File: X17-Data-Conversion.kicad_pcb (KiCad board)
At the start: 2 copper layers, 26 parts, among them J1 Conn_01x05, U2 STM32F091CCTx, U3 MAX485E

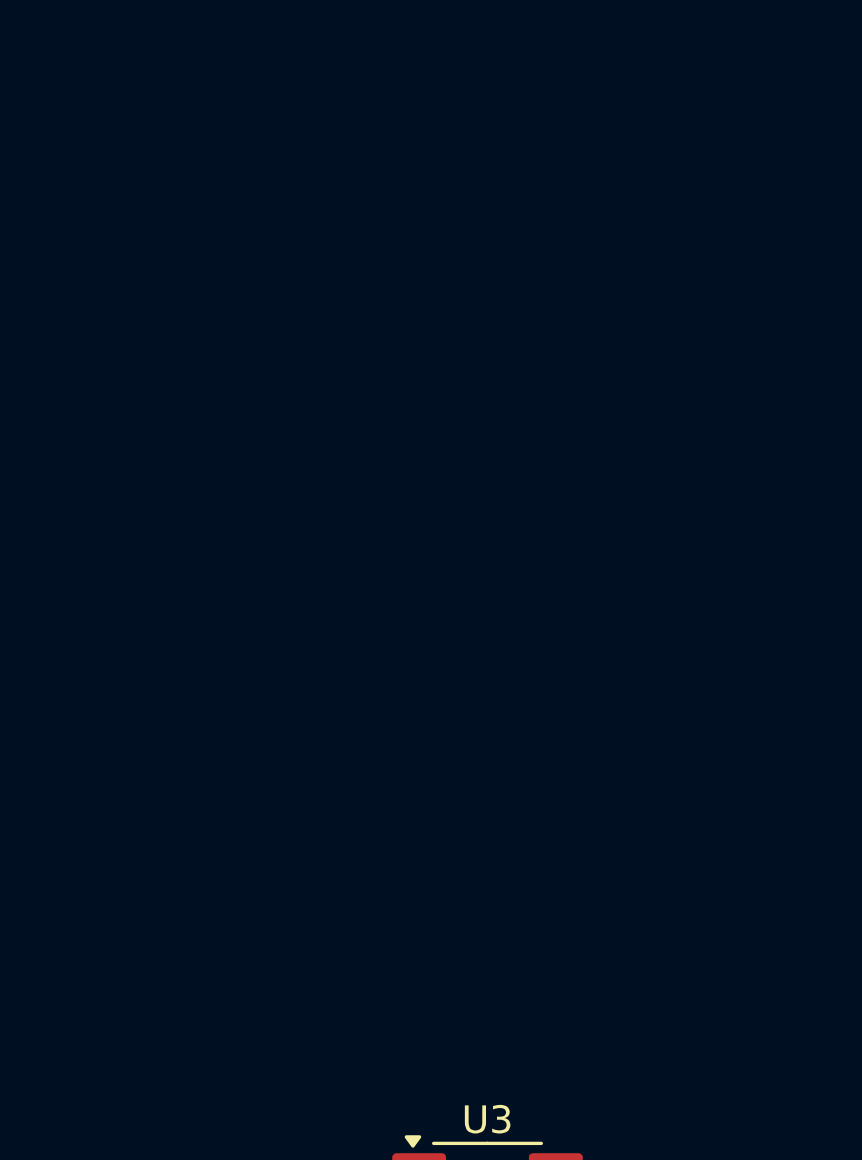
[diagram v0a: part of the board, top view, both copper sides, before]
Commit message: All Layout points are fixed
the layout now has all the components without errors or warnings. However, GND and NRST are all connected.
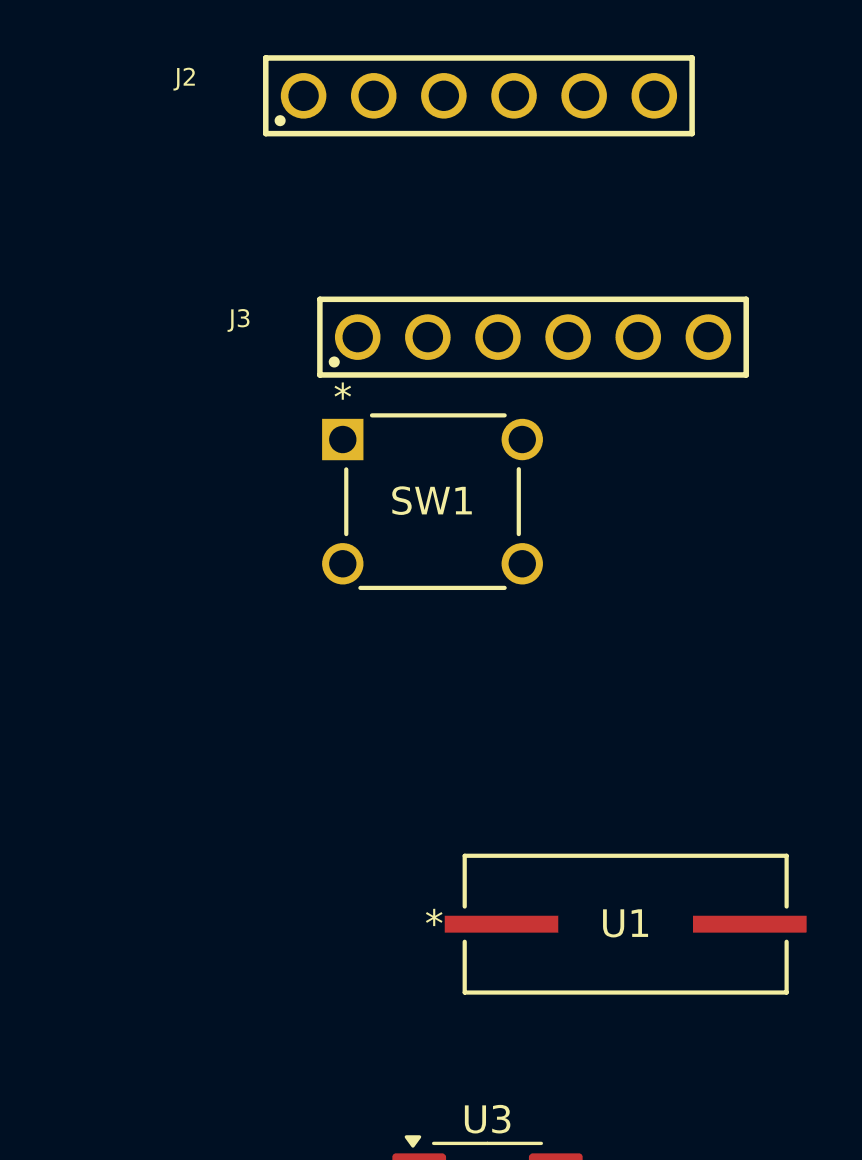
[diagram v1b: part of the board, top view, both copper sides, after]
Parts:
- added J2: BG030_-_-_-_6_-_-_X_-_XXX_-_-_REVG5, 61300611121:61300611121, F.Cu at (98.2, 27.5)
- added J3: BG030_-_-_-_6_-_-_X_-_XXX_-_-_REVG5, 61300611121:61300611121, F.Cu at (100.2, 36.2)
- added SW1: 1825910-6, footprints1:SW4_1825910-B_TEC, F.Cu at (99.8, 44.4)
- added U1: ABLS-8.000MHZ-B2-T, footprints2:ABLS-8.000MHZ-B2-T_ABR, F.Cu at (103.5, 57.5)

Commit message: Updates
Now the GND and NRST are not fully interconnected and overlapping each others signals.
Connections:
- C1 pad 1: Net-(C1-Pad1) -> NRST_PSB
- C1 pad 2: NRST_PSB -> GND
- C10 pad 2: NRST_PSB -> GND
- C11 pad 2: NRST_PSB -> GND
- C2 pad 2: NRST_PSB -> GND
- C3 pad 2: NRST_PSB -> GND
- C4 pad 1: NRST_PSB -> GND
- C5 pad 1: NRST_PSB -> GND
- C6 pad 1: NRST_PSB -> GND
- C7 pad 1: NRST_PSB -> GND
- C8 pad 1: NRST_PSB -> GND
- C9 pad 1: NRST_PSB -> GND
- D1 pad 1: NRST_PSB -> GND
- J1 pad 3: NRST_PSB -> GND
- J2 pad 2: NRST_PSB -> GND
- J3 pad 1: NRST_PSB -> GND
- R1 pad 2: Net-(C1-Pad1) -> NRST_PSB
- R10 pad 2: NRST_PSB -> GND
- SW1 pad 1: Net-(C1-Pad1) -> NRST_PSB
- SW1 pad 2: Net-(C1-Pad1) -> NRST_PSB
- SW1 pad 3: NRST_PSB -> GND
- SW1 pad 4: NRST_PSB -> GND
- U2 pad 23: NRST_PSB -> GND
- U2 pad 35: NRST_PSB -> GND
- U2 pad 44: NRST_PSB -> GND
- U2 pad 45: NRST_PSB -> GND
- U2 pad 47: NRST_PSB -> GND
- U2 pad 8: NRST_PSB -> GND
- U3 pad 5: NRST_PSB -> GND

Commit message: Layout is somewhat laid out.
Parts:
- moved C11 108.3 mm to (171.5, 101.9), turned to 90 degrees
- moved R10 107.8 mm to (177.0, 101.5)
- moved R9 107.2 mm to (177.0, 97.0)
- moved C10 105.0 mm to (166.5, 101.9), turned to 90 degrees
- moved R11 104.9 mm to (177.0, 92.5)
- moved C1 100.3 mm to (144.0, 100.1), turned to -90 degrees
- moved D1 98.7 mm to (156.0, 69.5)
- moved R8 94.8 mm to (159.6, 105.5)
- moved R7 94.0 mm to (159.6, 101.0)
- moved R6 93.2 mm to (159.6, 96.5)
- moved R3 92.5 mm to (151.0, 88.0), turned to 90 degrees
- moved R5 92.3 mm to (159.5, 92.0)
- moved C9 90.3 mm to (134.6, 111.0)
- moved R1 90.0 mm to (144.0, 95.5), turned to 90 degrees
- moved J1 89.7 mm to (177.0, 81.2), turned to 180 degrees
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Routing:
- added copper zone on F.Cu, net 3.3V
- added copper zone on B.Cu, net GND
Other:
- board outline added: 56.5 x 55.5 mm

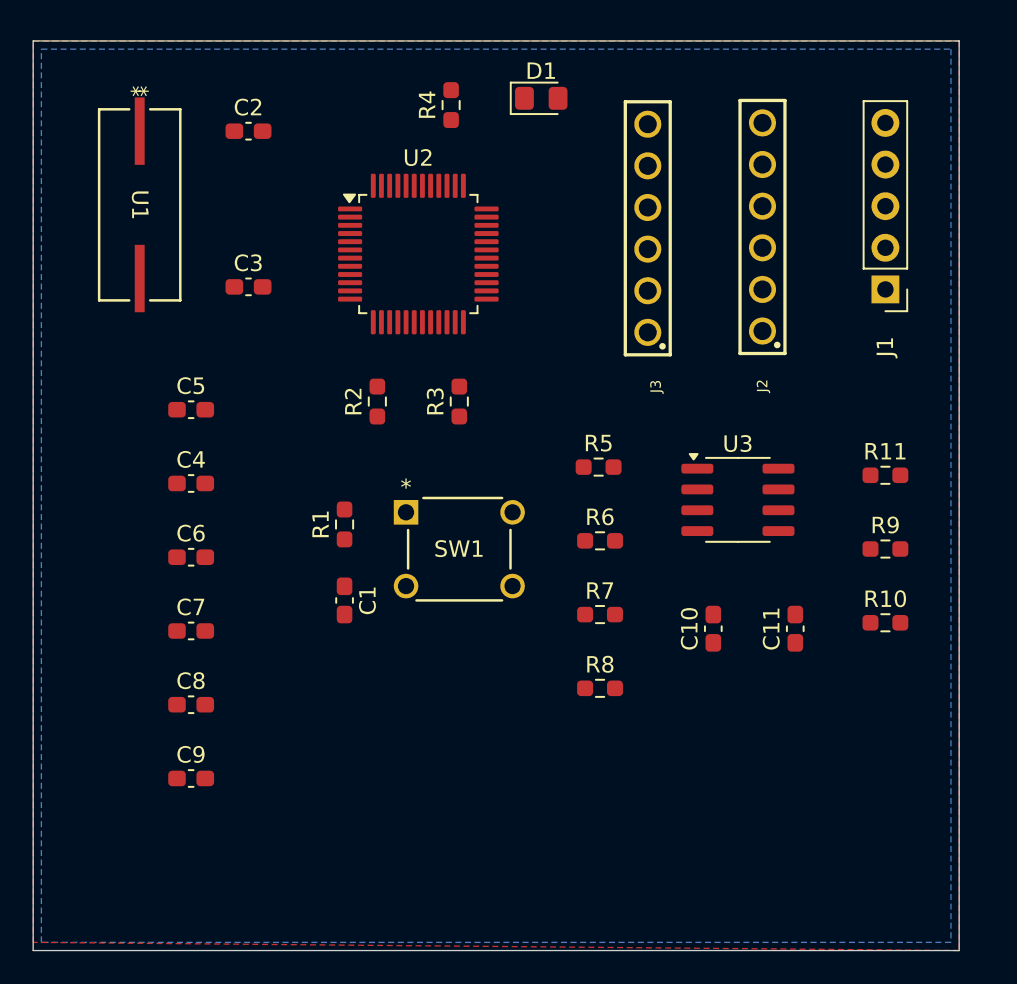
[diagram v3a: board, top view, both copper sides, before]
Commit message: 3.3V and GND is whats left
All my changes are included. All layout is finished except for 3.3V and GND
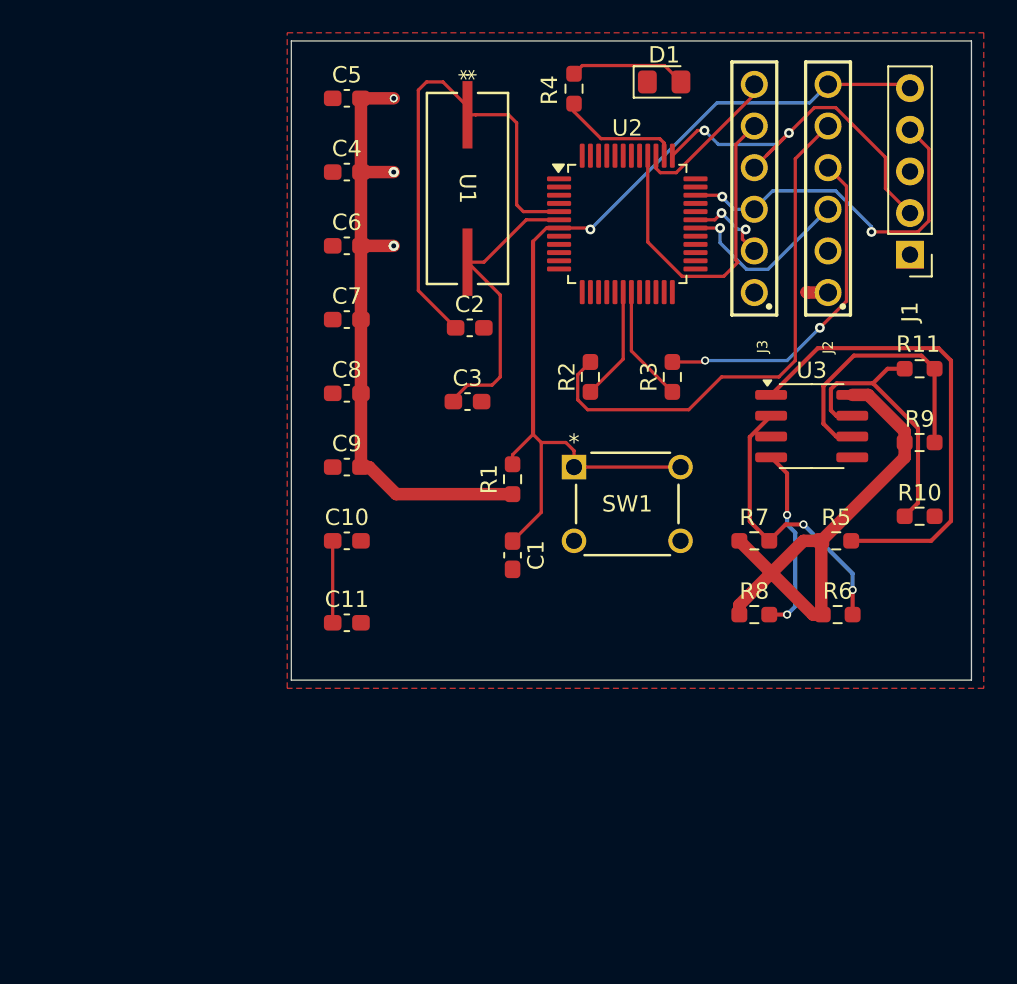
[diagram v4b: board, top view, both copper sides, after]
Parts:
- moved C11 27.4 mm to (144.1, 101.5), turned to 0 degrees
- moved C10 23.0 mm to (144.1, 96.5), turned to 0 degrees
- moved C4 21.2 mm to (144.1, 74.0)
- moved C5 21.2 mm to (144.1, 69.5)
- moved C6 21.2 mm to (144.1, 78.5)
- moved C7 21.2 mm to (144.1, 83.0)
- moved C8 21.2 mm to (144.1, 87.5)
- moved C9 21.2 mm to (144.1, 92.0)
- moved U1 20.0 mm to (151.5, 75.0)
- moved C2 18.1 mm to (151.6, 83.5)
- moved R5 15.2 mm to (174.0, 96.5)
- moved R6 15.2 mm to (174.1, 101.0)
- moved C3 15.1 mm to (151.5, 88.0)
- moved R2 13.1 mm to (159.0, 86.5)
- moved R3 13.1 mm to (164.0, 86.5)
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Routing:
- net NRST_PSB: track 0.00 -> 58.4 mm, vias 0 -> 1
- net 3.3V: track 0.00 -> 39.8 mm, vias 0 -> 3
- net C2_1: track 0.00 -> 32.5 mm
- net 5V: track 0.00 -> 31.6 mm
- net /OSC_IN: track 0.00 -> 30.7 mm
- net USART1_RX: track 0.00 -> 28.8 mm
- net SWCLK: track 0.00 -> 27.0 mm, vias 0 -> 2
- net SWDIO: track 0.00 -> 22.9 mm, vias 0 -> 2
- net ALERT1: track 0.00 -> 20.8 mm
- net C2_2: track 0.00 -> 20.8 mm, vias 0 -> 2
- net /OSC_OUT: track 0.00 -> 18.1 mm
- net USART1_DE: track 0.00 -> 17.9 mm, vias 0 -> 2
- net A-: track 0.00 -> 17.3 mm
- net A+: track 0.00 -> 16.8 mm
- net USART1_TX: track 0.00 -> 11.5 mm, vias 0 -> 2
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- added copper zone on F.Cu, net GND
- removed copper zone on F.Cu, net 3.3V
- removed copper zone on B.Cu, net GND
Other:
- board size 56.5 x 55.5 mm -> 41.5 x 39 mm

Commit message: included name
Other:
- board text added: "12/26/2024"
- board text added: "X17 Data Conversion"
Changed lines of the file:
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@@
 		(pad_to_mask_clearance 0)
 		(allow_soldermask_bridges_in_footprints no)
-		(grid_origin 125 121.5)
+		(grid_origin 140.75 105)
 		(pcbplotparams
 			(layerselection 0x00010fc_ffffffff)
@@
 		(layer "Edge.Cuts")
 	)
+	(gr_text "X17 Data Conversion\n"
+		(at 186.25 190 0)
+		(layer "Dwgs.User")
+		(effects
+			(font
+				(size 1 1)
+				(thickness 0.15)
+			)
+			(justify left bottom)
+		)
+	)
+	(gr_text "12/26/2024\n"
+		(at 208.25 194 0)
+		(layer "Dwgs.User")
+		(effects
+			(font
+				(size 1 1)
+				(thickness 0.15)
+			)
+			(justify left bottom)
+		)
+	)
 	(segment

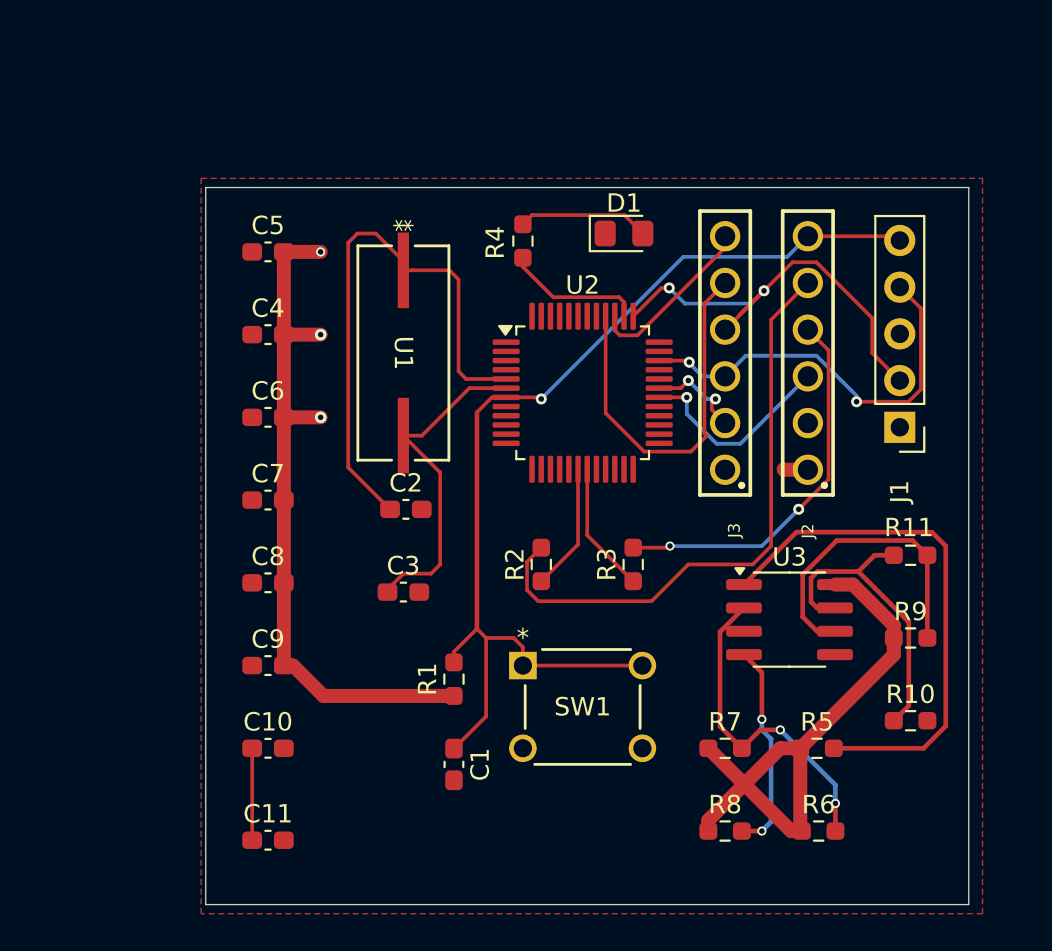
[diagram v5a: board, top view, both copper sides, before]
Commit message: DRC process
3 errors
4 warnings
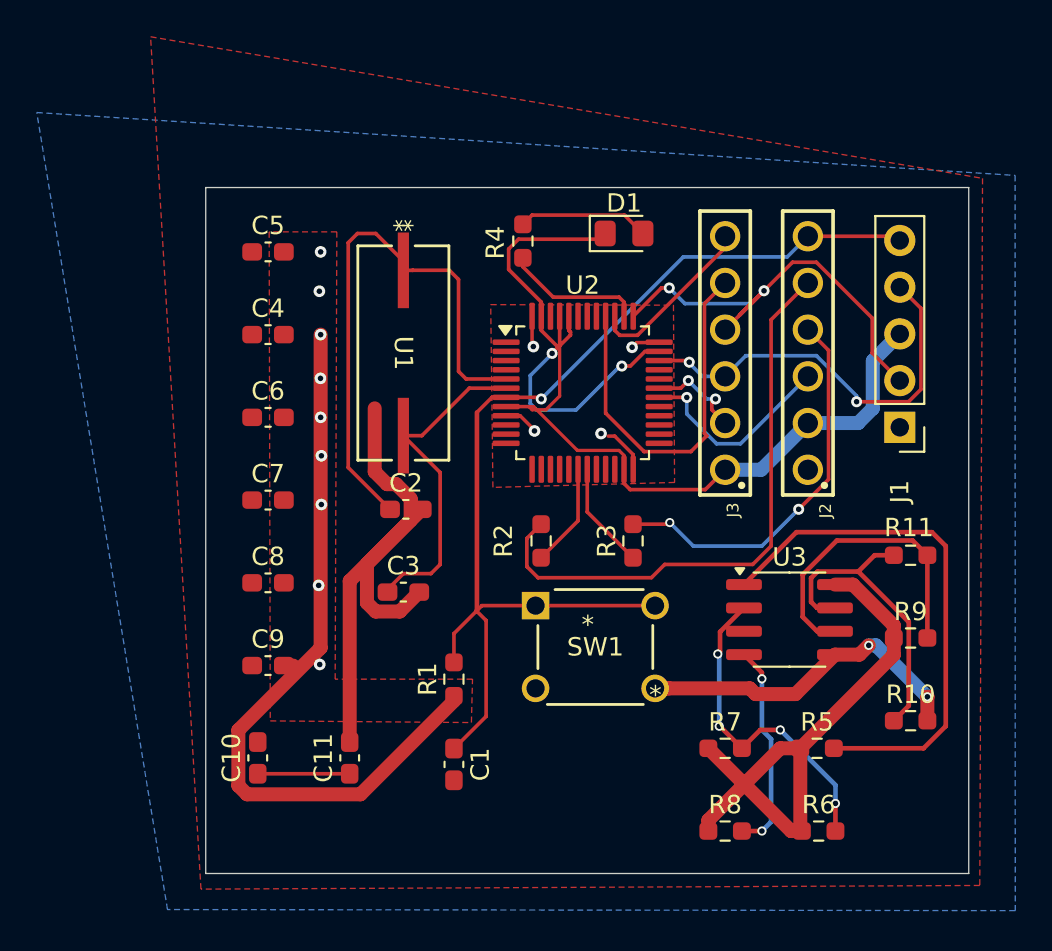
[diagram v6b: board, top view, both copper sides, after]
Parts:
- moved C11 6.31 mm to (148.6, 97.0), turned to 90 degrees
- moved SW1 3.33 mm to (165.2, 93.2)
- moved R2 1.28 mm to (159.0, 85.2)
- moved R3 1.28 mm to (164.0, 85.2)
- moved C10 0.76 mm to (143.6, 97.0), turned to 90 degrees
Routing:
- net GND: track 0.00 -> 113.0 mm, vias 0 -> 4
- net 3.3V: track 39.8 -> 48.5 mm, vias 3 -> 13
- net Net-(U2-PB1): track 7.12 -> 5.84 mm
- net Net-(U2-PB0): track 6.92 -> 5.66 mm
- net NRST_PSB: track 58.4 -> 59.5 mm
- net C2_2: track 20.8 -> 21.3 mm
- net C2_1: track 32.5 -> 32.0 mm
- net USART1_DE: track 17.9 -> 18.0 mm, vias 2 -> 4
- added copper zone on B.Cu, net 3.3V
- added copper zone on F.Cu, net 3.3V
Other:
- board size 41.5 x 39 mm -> 41.5 x 37.3 mm
